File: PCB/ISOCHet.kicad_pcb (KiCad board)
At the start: 2 copper layers, 57.1 x 38.1 mm, 19 parts, among them J1 USB_C_Receptacle_USB2.0, J2 Conn_01x08_Pin, SW0 BOOT, SW1 TAB, SW2 ENTER, SW3 CAPS, SW4 CAPS_STEP1.5, SW5 CAPS_STEP1.25, U1 CH552E, U2 USBLC6-2P6

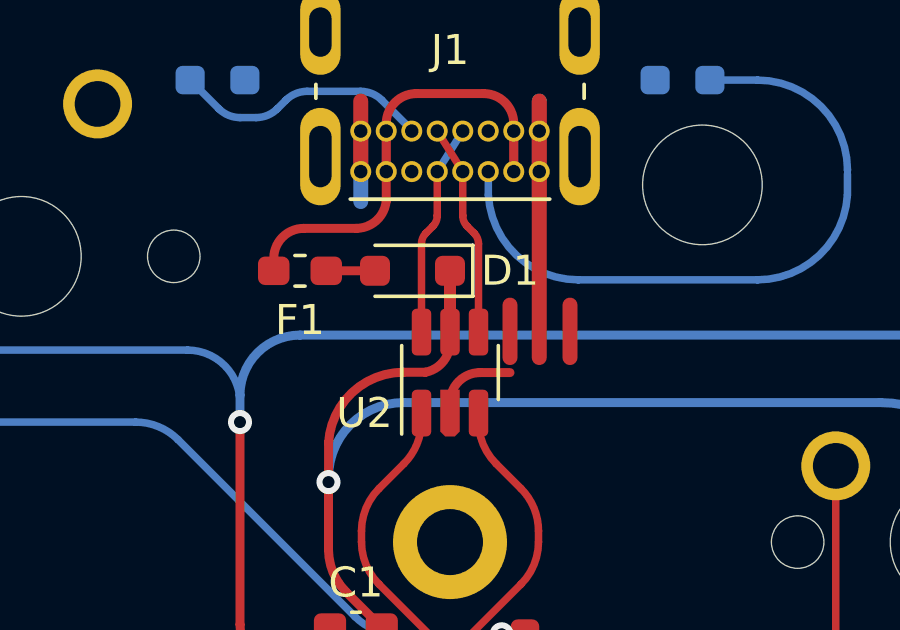
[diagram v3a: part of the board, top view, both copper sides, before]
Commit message: Round outside corners of keep-out areas
KiCad only seems to round the inside corners, so some arcs on the GND net are added.
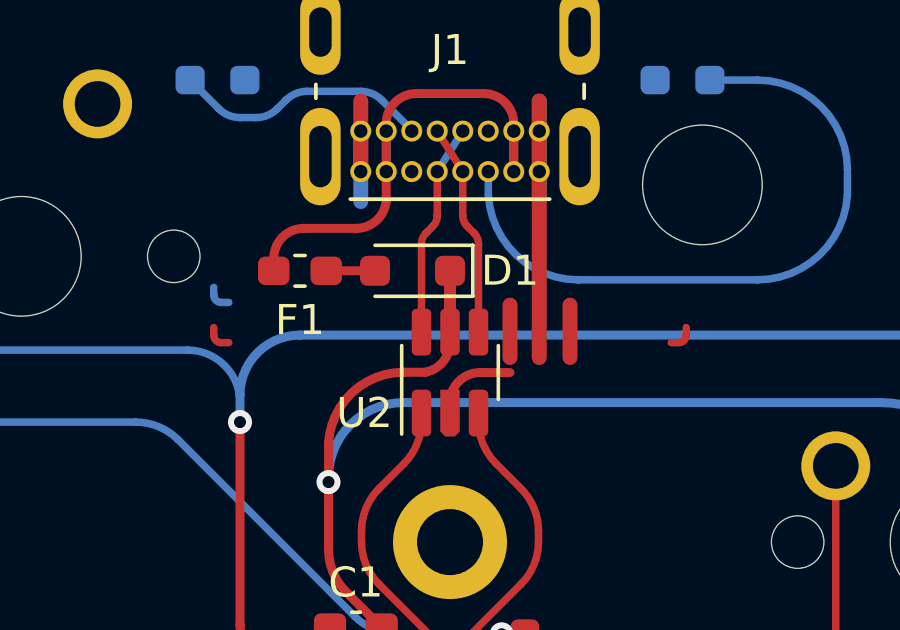
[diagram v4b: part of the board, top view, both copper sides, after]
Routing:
- net GND: track 24.5 -> 27.1 mm
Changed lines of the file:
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@@
   (arc (start 157.2 52.5) (mid 155.432233 53.232233) (end 154.7 55) (width 0.3) (layer "B.Cu") (net 1))
   (arc (start 176.228427 53.978427) (mid 177.52612 54.845518) (end 179.056854 55.15) (width 0.3) (layer "B.Cu") (net 1))
+  (segment (start 150.875 50) (end 150.875 50.25) (width 0.25) (layer "F.Cu") (net 2))
   (segment (start 161.725 42.45) (end 161.725 51) (width 0.5) (layer "F.Cu") (net 2))
   (segment (start 160.75 51.5) (end 159.75 51.5) (width 0.3) (layer "F.Cu") (net 2))
@@
   (segment (start 158 63.75) (end 158 61.895) (width 0.3) (layer "F.Cu") (net 2))
   (segment (start 155.775 42.45) (end 155.775 44.8) (width 0.5) (layer "F.Cu") (net 2))
+  (segment (start 166.625 50.25) (end 166.625 50) (width 0.25) (layer "F.Cu") (net 2))
+  (segment (start 151.125 50.5) (end 151.375 50.5) (width 0.25) (layer "F.Cu") (net 2))
   (segment (start 160.75 51) (end 160.75 49.25) (width 0.5) (layer "F.Cu") (net 2))
+  (segment (start 166.125 50.5) (end 166.375 50.5) (width 0.25) (layer "F.Cu") (net 2))
+  (arc (start 151.125 50.5) (mid 150.948223 50.426777) (end 150.875 50.25) (width 0.25) (layer "F.Cu") (net 2))
+  (arc (start 166.625 50.25) (mid 166.551777 50.426777) (end 166.375 50.5) (width 0.25) (layer "F.Cu") (net 2))
   (arc (start 159.75 51.5) (mid 159.042893 51.792893) (end 158.75 52.5) (width 0.3) (layer "F.Cu") (net 2))
+  (segment (start 150.875 48.66125) (end 150.875 48.91125) (width 0.25) (layer "B.Cu") (net 2))
   (segment (start 161.725 42.45) (end 161.725 45.8) (width 0.5) (layer "B.Cu") (net 2))
+  (segment (start 151.125 49.16125) (end 151.375 49.16125) (width 0.25) (layer "B.Cu") (net 2))
   (segment (start 155.775 43.45) (end 155.775 45.8) (width 0.5) (layer "B.Cu") (net 2))
+  (arc (start 151.125 49.16125) (mid 150.948223 49.088027) (end 150.875 48.91125) (width 0.25) (layer "B.Cu") (net 2))
   (segment (start 154.625 48.1075) (end 156.25 48.1075) (width 0.3) (layer "F.Cu") (net 3))
   (segment (start 160.875 43.45) (end 160.875 43.2) (width 0.3) (layer "F.Cu") (net 4))
@@
         (xy 162.75 48.5375)
         (xy 162.75 49.0375)
-        (xy 151.25 49.0375)
-        (xy 151 48.7625)
+        (xy 151 49.0375)
         (xy 151 42.5375)
       )

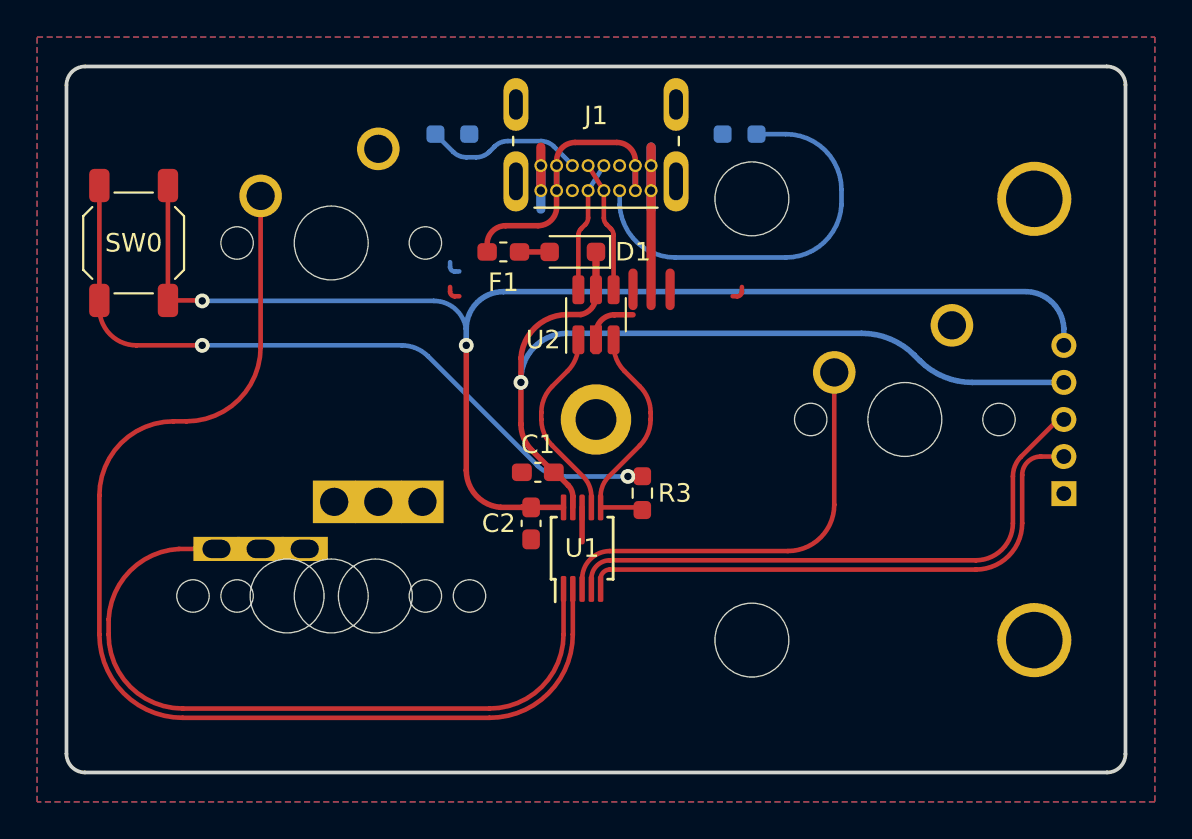
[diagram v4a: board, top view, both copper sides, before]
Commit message: Reroute UDP to Boot switch tracks
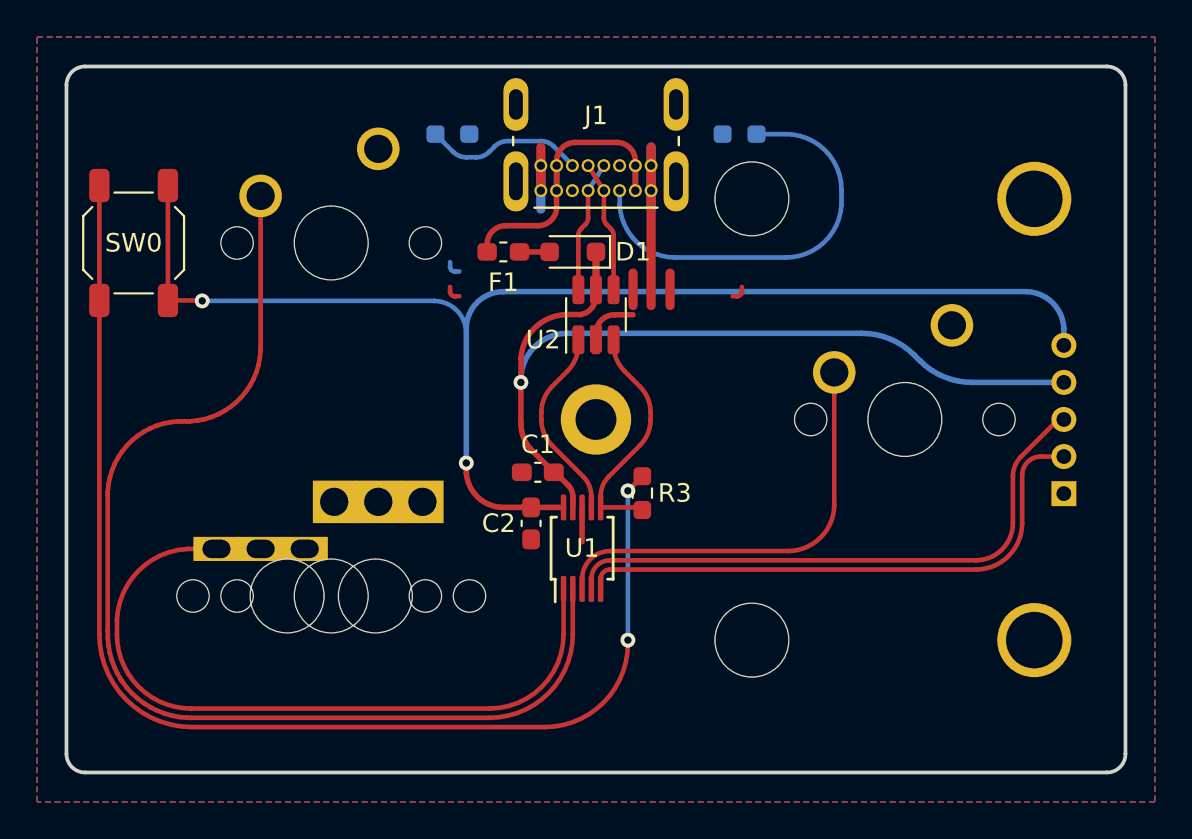
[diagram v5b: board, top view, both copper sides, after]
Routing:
- net Net-(R3-Pad2): track 39.3 -> 67.1 mm
- net +3V3: track 73.1 -> 79.5 mm
